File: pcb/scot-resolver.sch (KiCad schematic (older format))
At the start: 8 parts, among them J1 Conn_01x02_Female, J2 Conn_01x02_Female, J3 Conn_01x02_Female, J4 Conn_01x03_Female, J5 Conn_01x03_Female, J6 Conn_01x03_Female

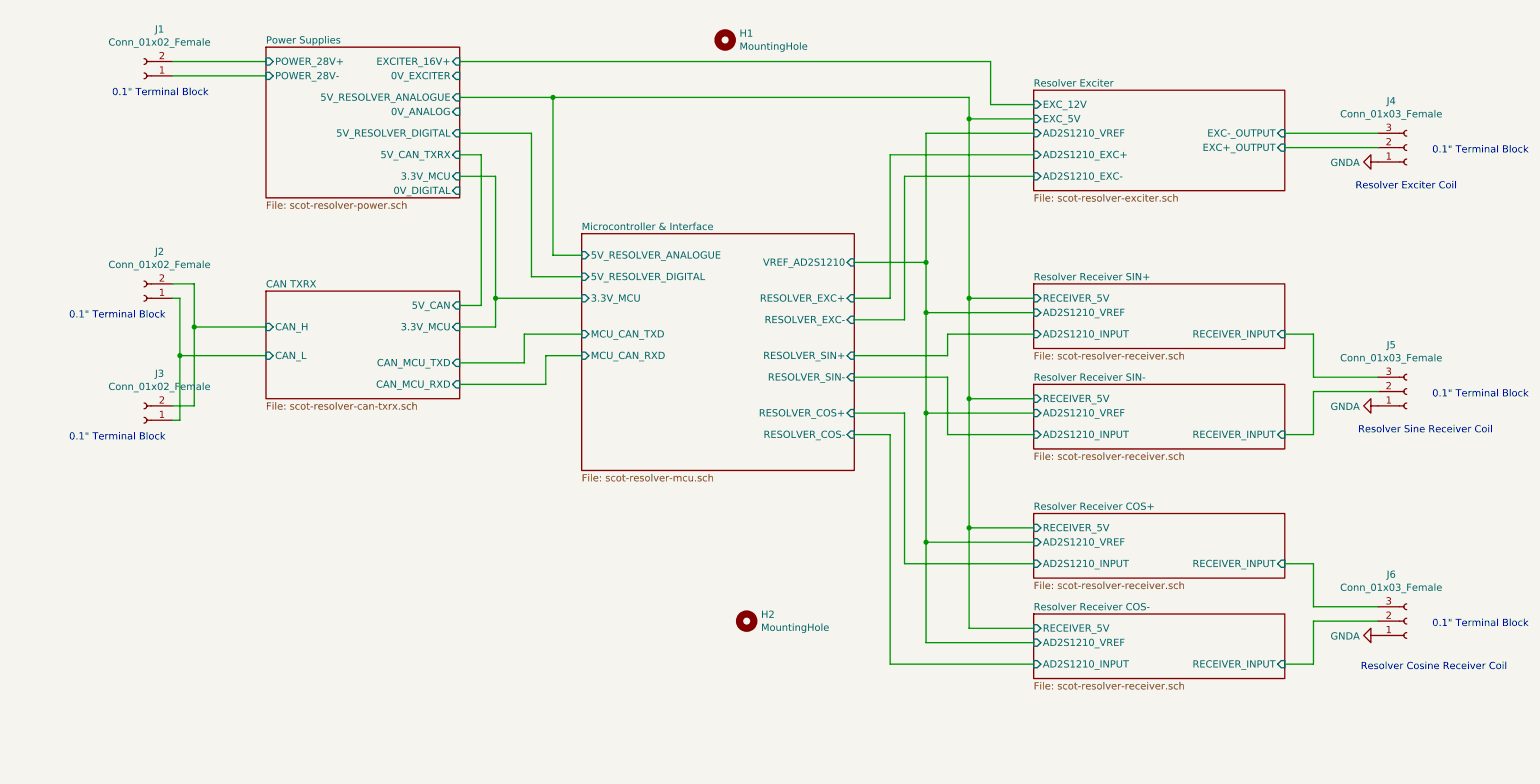
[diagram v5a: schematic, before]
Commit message: pcb: V2 schematic updates (PCB still to do).
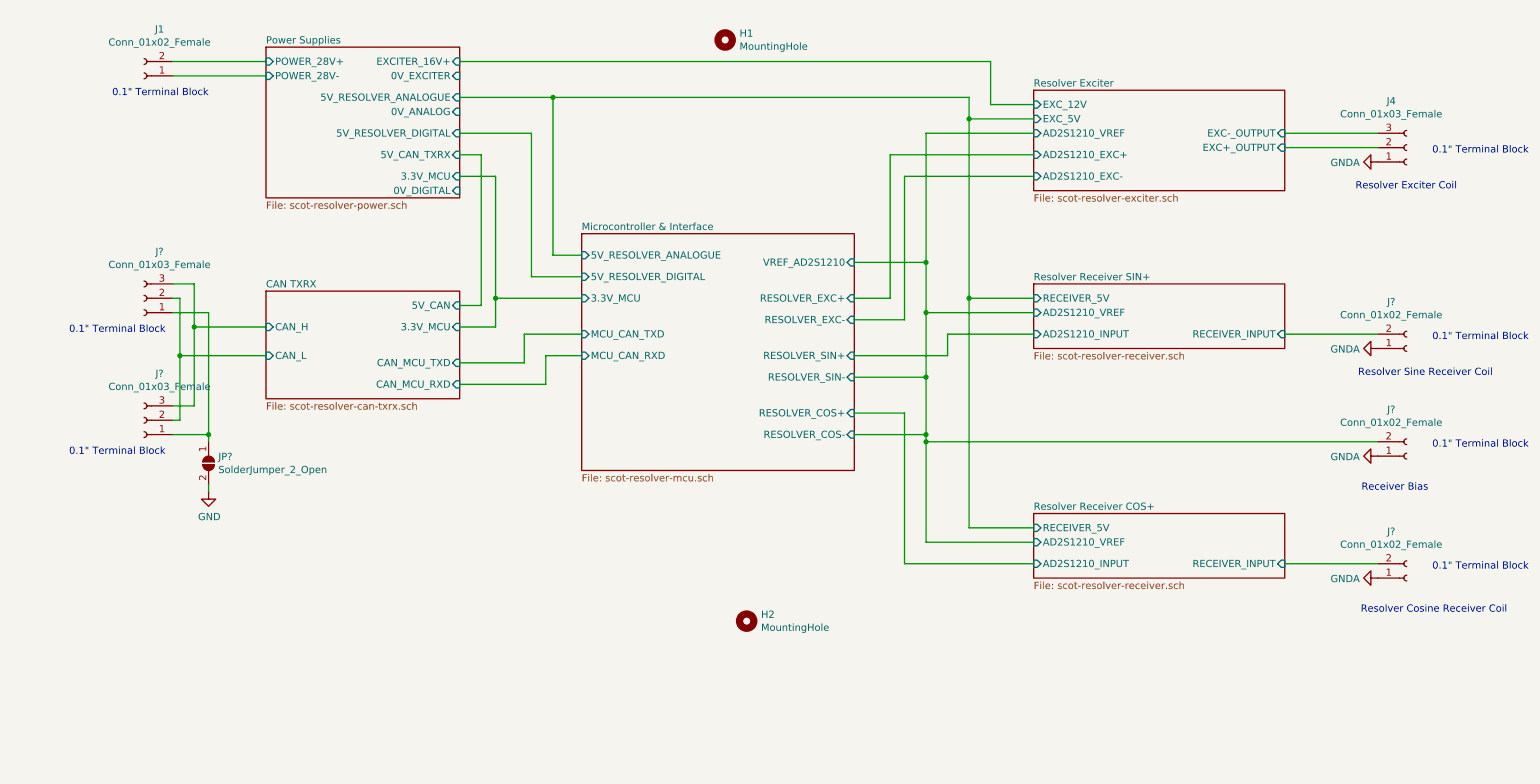
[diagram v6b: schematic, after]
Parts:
- removed J2, J3: Conn_01x02_Female, TerminalBlock_TE-Connectivity:TerminalBlock_TE_282834-2_1x02_P2.54mm_Horizontal, symbol Connector:Conn_01x02_Female
- removed J5, J6: Conn_01x03_Female, TerminalBlock_TE-Connectivity:TerminalBlock_TE_282834-3_1x03_P2.54mm_Horizontal, symbol Connector:Conn_01x03_Female
- added J? (x3): Conn_01x02_Female, TerminalBlock_TE-Connectivity:TerminalBlock_TE_282834-2_1x02_P2.54mm_Horizontal, symbol Connector:Conn_01x02_Female
- added J? (x2): Conn_01x03_Female, TerminalBlock_TE-Connectivity:TerminalBlock_TE_282834-3_1x03_P2.54mm_Horizontal, symbol Connector:Conn_01x03_Female
- added JP?: SolderJumper_2_Open, symbol Jumper:SolderJumper_2_Open
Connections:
- net CAN TXRX/CAN_H: now also J?.3 (Pin_3), J?.3 (Pin_3)
- net CAN TXRX/CAN_L: now also J?.2 (Pin_2), J?.2 (Pin_2)
- net GNDA: now also J?.1 (Pin_1), J?.1 (Pin_1), J?.1 (Pin_1)
- net Microcontroller & Interface/RESOLVER_COS-: now also J?.2 (Pin_2)
- net Resolver Receiver COS+/RECEIVER_INPUT: now also J?.2 (Pin_2)
- net Resolver Receiver SIN+/RECEIVER_INPUT: now also J?.2 (Pin_2)
- new net: J?.1 (Pin_1), J?.1 (Pin_1), JP?.1 (A)
- new net GND: JP?.2 (B)
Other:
- note added: "Receiver Bias"
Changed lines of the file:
@@
 $Descr A4 11693 8268
 encoding utf-8
-Sheet 1 9
+Sheet 1 7
 Title ""
 Date ""
@@
 Comment4 ""
 $EndDescr
-$Comp
-L Connector:Conn_01x02_Female J2
-U 1 1 5E03E563
-P 1350 2700
-F 0 "J2" H 1242 2375 50  0000 C CNN
-F 1 "Conn_01x02_Female" H 1242 2466 50  0000 C CNN
-F 2 "TerminalBlock_TE-Connectivity:TerminalBlock_TE_282834-2_1x02_P2.54mm_Horizontal" H 1350 2700 50  0001 C CNN
-F 3 "~" H 1350 2700 50  0001 C CNN
-	1    1350 2700
-	-1   0    0    1
-$EndComp
-$Comp
-L Connector:Conn_01x02_Female J3
-U 1 1 5E03F192
-P 1350 3550
-F 0 "J3" H 1242 3225 50  0000 C CNN
-F 1 "Conn_01x02_Female" H 1242 3316 50  0000 C CNN
-F 2 "TerminalBlock_TE-Connectivity:TerminalBlock_TE_282834-2_1x02_P2.54mm_Horizontal" H 1350 3550 50  0001 C CNN
-F 3 "~" H 1350 3550 50  0001 C CNN
-	1    1350 3550
-	-1   0    0    1
-$EndComp
 Wire Wire Line
 	1550 3450 1700 3450
@@
 	9300 1650 9950 1650
 $Sheet
-S 7550 3300 1750 450
-U 5E46BA7D
-F0 "Resolver Receiver SIN-" 50
-F1 "scot-resolver-receiver.sch" 50
-F2 "RECEIVER_INPUT" I R 9300 3650 50
-F3 "AD2S1210_VREF" I L 7550 3500 50
-F4 "AD2S1210_INPUT" I L 7550 3650 50
-F5 "RECEIVER_5V" I L 7550 3400 50
-$EndSheet
-$Sheet
 S 7550 4200 1750 450
 U 5E46F57D
@@
 F5 "RECEIVER_5V" I L 7550 4300 50
 $EndSheet
-$Sheet
-S 7550 4900 1750 450
-U 5E46F583
-F0 "Resolver Receiver COS-" 50
-F1 "scot-resolver-receiver.sch" 50
-F2 "RECEIVER_INPUT" I R 9300 5250 50
-F3 "AD2S1210_VREF" I L 7550 5100 50
-F4 "AD2S1210_INPUT" I L 7550 5250 50
-F5 "RECEIVER_5V" I L 7550 5000 50
-$EndSheet
-Wire Wire Line
-	9500 3250 9500 2950
-Wire Wire Line
-	9500 2950 9300 2950
-Wire Wire Line
-	9500 3350 9500 3650
-Wire Wire Line
-	9500 3650 9300 3650
-Wire Wire Line
-	9500 4850 9500 4550
-Wire Wire Line
-	9500 4550 9300 4550
-Wire Wire Line
-	9500 4950 9500 5250
-Wire Wire Line
-	9500 5250 9300 5250
 $Sheet
 S 2200 2650 1350 750
@@
 	7100 2700 7550 2700
 Connection ~ 7100 1450
-Wire Wire Line
-	7100 2700 7100 3400
-Wire Wire Line
-	7100 3400 7550 3400
 Connection ~ 7100 2700
 Wire Wire Line
-	7100 3400 7100 4300
-Wire Wire Line
 	7100 4300 7550 4300
-Connection ~ 7100 3400
-Wire Wire Line
-	7100 4300 7100 5000
-Wire Wire Line
-	7100 5000 7550 5000
-Connection ~ 7100 4300
 $Sheet
 S 4400 2250 1900 1650
@@
 	6800 2800 7550 2800
 Connection ~ 6800 2450
-Wire Wire Line
-	6800 2800 6800 3500
-Wire Wire Line
-	6800 3500 7550 3500
 Connection ~ 6800 2800
 Wire Wire Line
-	6800 3500 6800 4400
-Wire Wire Line
 	6800 4400 7550 4400
-Connection ~ 6800 3500
-Wire Wire Line
-	6800 4400 6800 5100
-Wire Wire Line
-	6800 5100 7550 5100
-Connection ~ 6800 4400
 Wire Wire Line
 	6300 3500 6650 3500
@@
 Wire Wire Line
 	6650 4550 7550 4550
-Wire Wire Line
-	7550 5250 6550 5250
-Wire Wire Line
-	6550 5250 6550 3650
-Wire Wire Line
-	6550 3650 6300 3650
-Wire Wire Line
-	6300 3250 6950 3250
-Wire Wire Line
-	6950 3250 6950 3650
-Wire Wire Line
-	6950 3650 7550 3650
 Wire Wire Line
 	6300 3100 6950 3100
@@
 Text Notes 10500 1950 2    50   ~ 0
 Resolver Exciter Coil
-Text Notes 10750 3650 2    50   ~ 0
+Text Notes 10750 3250 2    50   ~ 0
 Resolver Sine Receiver Coil
-Text Notes 10850 5300 2    50   ~ 0
+Text Notes 10850 4900 2    50   ~ 0
 Resolver Cosine Receiver Coil
 Wire Wire Line
@@
 	0    1    1    0
 $EndComp
-Wire Wire Line
-	9500 3250 9950 3250
-Wire Wire Line
-	9950 3350 9500 3350
 $Comp
 L power:GNDA #PWR0102
 U 1 1 5E62D3A8
-P 9950 3450
-F 0 "#PWR0102" H 9950 3200 50  0001 C CNN
-F 1 "GNDA" V 9955 3323 50  0000 R CNN
-F 2 "" H 9950 3450 50  0001 C CNN
-F 3 "" H 9950 3450 50  0001 C CNN
-	1    9950 3450
+P 9950 3050
+F 0 "#PWR0102" H 9950 2800 50  0001 C CNN
+F 1 "GNDA" V 9955 2923 50  0000 R CNN
+F 2 "" H 9950 3050 50  0001 C CNN
+F 3 "" H 9950 3050 50  0001 C CNN
+	1    9950 3050
 	0    1    1    0
 $EndComp
@@
 L power:GNDA #PWR0103
 U 1 1 5E638B63
-P 9950 5050
-F 0 "#PWR0103" H 9950 4800 50  0001 C CNN
-F 1 "GNDA" V 9955 4923 50  0000 R CNN
-F 2 "" H 9950 5050 50  0001 C CNN
-F 3 "" H 9950 5050 50  0001 C CNN
-	1    9950 5050
+P 9950 4650
+F 0 "#PWR0103" H 9950 4400 50  0001 C CNN
+F 1 "GNDA" V 9955 4523 50  0000 R CNN
+F 2 "" H 9950 4650 50  0001 C CNN
+F 3 "" H 9950 4650 50  0001 C CNN
+	1    9950 4650
 	0    1    1    0
 $EndComp
-Wire Wire Line
-	9950 4950 9500 4950
-Wire Wire Line
-	9500 4850 9950 4850
 $Comp
 L Connector:Conn_01x03_Female J4
@@
 $EndComp
 $Comp
-L Connector:Conn_01x03_Female J5
-U 1 1 5E642718
-P 10150 3350
-F 0 "J5" H 10042 3025 50  0000 C CNN
-F 1 "Conn_01x03_Female" H 10042 3116 50  0000 C CNN
-F 2 "TerminalBlock_TE-Connectivity:TerminalBlock_TE_282834-3_1x03_P2.54mm_Horizontal" H 10150 3350 50  0001 C CNN
-F 3 "~" H 10150 3350 50  0001 C CNN
-	1    10150 3350
-	1    0    0    1
-$EndComp
-$Comp
-L Connector:Conn_01x03_Female J6
-U 1 1 5E642DF1
-P 10150 4950
-F 0 "J6" H 10042 4625 50  0000 C CNN
-F 1 "Conn_01x03_Female" H 10042 4716 50  0000 C CNN
-F 2 "TerminalBlock_TE-Connectivity:TerminalBlock_TE_282834-3_1x03_P2.54mm_Horizontal" H 10150 4950 50  0001 C CNN
-F 3 "~" H 10150 4950 50  0001 C CNN
-	1    10150 4950
-	1    0    0    1
-$EndComp
-$Comp
 L Mechanical:MountingHole H1
 U 1 1 5E4FCB16
@@
 	1    0    0    -1
 $EndComp
-Text Notes 1500 2850 2    50   ~ 0
-0.1" Terminal Block
-Text Notes 1500 3700 2    50   ~ 0
+Text Notes 1500 2950 2    50   ~ 0
+0.1" Terminal Block
+Text Notes 1500 3800 2    50   ~ 0
 0.1" Terminal Block
 Text Notes 11000 1700 2    50   ~ 0
 0.1" Terminal Block
-Text Notes 11000 3400 2    50   ~ 0
-0.1" Terminal Block
-Text Notes 11000 5000 2    50   ~ 0
-0.1" Terminal Block
+Text Notes 11000 3000 2    50   ~ 0
+0.1" Terminal Block
+Text Notes 11000 4600 2    50   ~ 0
+0.1" Terminal Block
+$Comp
+L Connector:Conn_01x02_Female J?
+U 1 1 5EAD507C
+P 10150 3050
+F 0 "J?" H 10042 2725 50  0000 C CNN
+F 1 "Conn_01x02_Female" H 10042 2816 50  0000 C CNN
+F 2 "TerminalBlock_TE-Connectivity:TerminalBlock_TE_282834-2_1x02_P2.54mm_Horizontal" H 10150 3050 50  0001 C CNN
+F 3 "~" H 10150 3050 50  0001 C CNN
+	1    10150 3050
+	1    0    0    1
+$EndComp
+Wire Wire Line
+	9300 2950 9950 2950
+$Comp
+L Connector:Conn_01x02_Female J?
+U 1 1 5EADF09C
+P 10150 4650
+F 0 "J?" H 10042 4325 50  0000 C CNN
+F 1 "Conn_01x02_Female" H 10042 4416 50  0000 C CNN
+F 2 "TerminalBlock_TE-Connectivity:TerminalBlock_TE_282834-2_1x02_P2.54mm_Horizontal" H 10150 4650 50  0001 C CNN
+F 3 "~" H 10150 4650 50  0001 C CNN
+	1    10150 4650
+	1    0    0    1
+$EndComp
+Wire Wire Line
+	9300 4550 9950 4550
+Text Notes 10300 4050 2    50   ~ 0
+Receiver Bias
+$Comp
+L power:GNDA #PWR?
+U 1 1 5EAE45AD
+P 9950 3800
+F 0 "#PWR?" H 9950 3550 50  0001 C CNN
+F 1 "GNDA" V 9955 3673 50  0000 R CNN
+F 2 "" H 9950 3800 50  0001 C CNN
+F 3 "" H 9950 3800 50  0001 C CNN
+	1    9950 3800
+	0    1    1    0
+$EndComp
+Text Notes 11000 3750 2    50   ~ 0
+0.1" Terminal Block
+$Comp
+L Connector:Conn_01x02_Female J?
+U 1 1 5EAE45B8
+P 10150 3800
+F 0 "J?" H 10042 3475 50  0000 C CNN
+F 1 "Conn_01x02_Female" H 10042 3566 50  0000 C CNN
+F 2 "TerminalBlock_TE-Connectivity:TerminalBlock_TE_282834-2_1x02_P2.54mm_Horizontal" H 10150 3800 50  0001 C CNN
+F 3 "~" H 10150 3800 50  0001 C CNN
+	1    10150 3800
+	1    0    0    1
+$EndComp
+Wire Wire Line
+	7100 2700 7100 4300
+Wire Wire Line
+	6800 2800 6800 3250
+Wire Wire Line
+	6800 3700 9950 3700
+Connection ~ 6800 3700
+Wire Wire Line
+	6800 3700 6800 4400
+Wire Wire Line
+	6300 3650 6800 3650
+Connection ~ 6800 3650
+Wire Wire Line
+	6800 3650 6800 3700
+Wire Wire Line
+	6300 3250 6800 3250
+Connection ~ 6800 3250
+Wire Wire Line
+	6800 3250 6800 3650
+$Comp
+L Connector:Conn_01x03_Female J?
+U 1 1 5EAEEF38
+P 1350 2700
+F 0 "J?" H 1242 2375 50  0000 C CNN
+F 1 "Conn_01x03_Female" H 1242 2466 50  0000 C CNN
+F 2 "TerminalBlock_TE-Connectivity:TerminalBlock_TE_282834-3_1x03_P2.54mm_Horizontal" H 1350 2700 50  0001 C CNN
+F 3 "~" H 1350 2700 50  0001 C CNN
+	1    1350 2700
+	-1   0    0    1
+$EndComp
+$Comp
+L Connector:Conn_01x03_Female J?
+U 1 1 5EAF204B
+P 1350 3550
+F 0 "J?" H 1242 3225 50  0000 C CNN
+F 1 "Conn_01x03_Female" H 1242 3316 50  0000 C CNN
+F 2 "TerminalBlock_TE-Connectivity:TerminalBlock_TE_282834-3_1x03_P2.54mm_Horizontal" H 1350 3550 50  0001 C CNN
+F 3 "~" H 1350 3550 50  0001 C CNN
+	1    1350 3550
+	-1   0    0    1
+$EndComp
+Wire Wire Line
+	1550 2800 1800 2800
+Wire Wire Line
+	1800 2800 1800 3650
+Wire Wire Line
+	1800 3650 1550 3650
+$Comp
+L Jumper:SolderJumper_2_Open JP?
+U 1 1 5EAF4284
+P 1800 3850
+F 0 "JP?" V 1754 3918 50  0000 L CNN
+F 1 "SolderJumper_2_Open" V 1845 3918 50  0000 L CNN
+F 2 "" H 1800 3850 50  0001 C CNN
+F 3 "~" H 1800 3850 50  0001 C CNN
+	1    1800 3850
+	0    1    1    0
+$EndComp
+$Comp
+L power:GND #PWR?
+U 1 1 5EAF4C43
+P 1800 4050
+F 0 "#PWR?" H 1800 3800 50  0001 C CNN
+F 1 "GND" H 1805 3877 50  0000 C CNN
+F 2 "" H 1800 4050 50  0001 C CNN
+F 3 "" H 1800 4050 50  0001 C CNN
+	1    1800 4050
+	1    0    0    -1
+$EndComp
+Wire Wire Line
+	1800 4050 1800 4000
+Wire Wire Line
+	1800 3700 1800 3650
+Connection ~ 1800 3650
 $EndSCHEMATC

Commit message: pcb: Add 10u to VREF, all 0402->0603
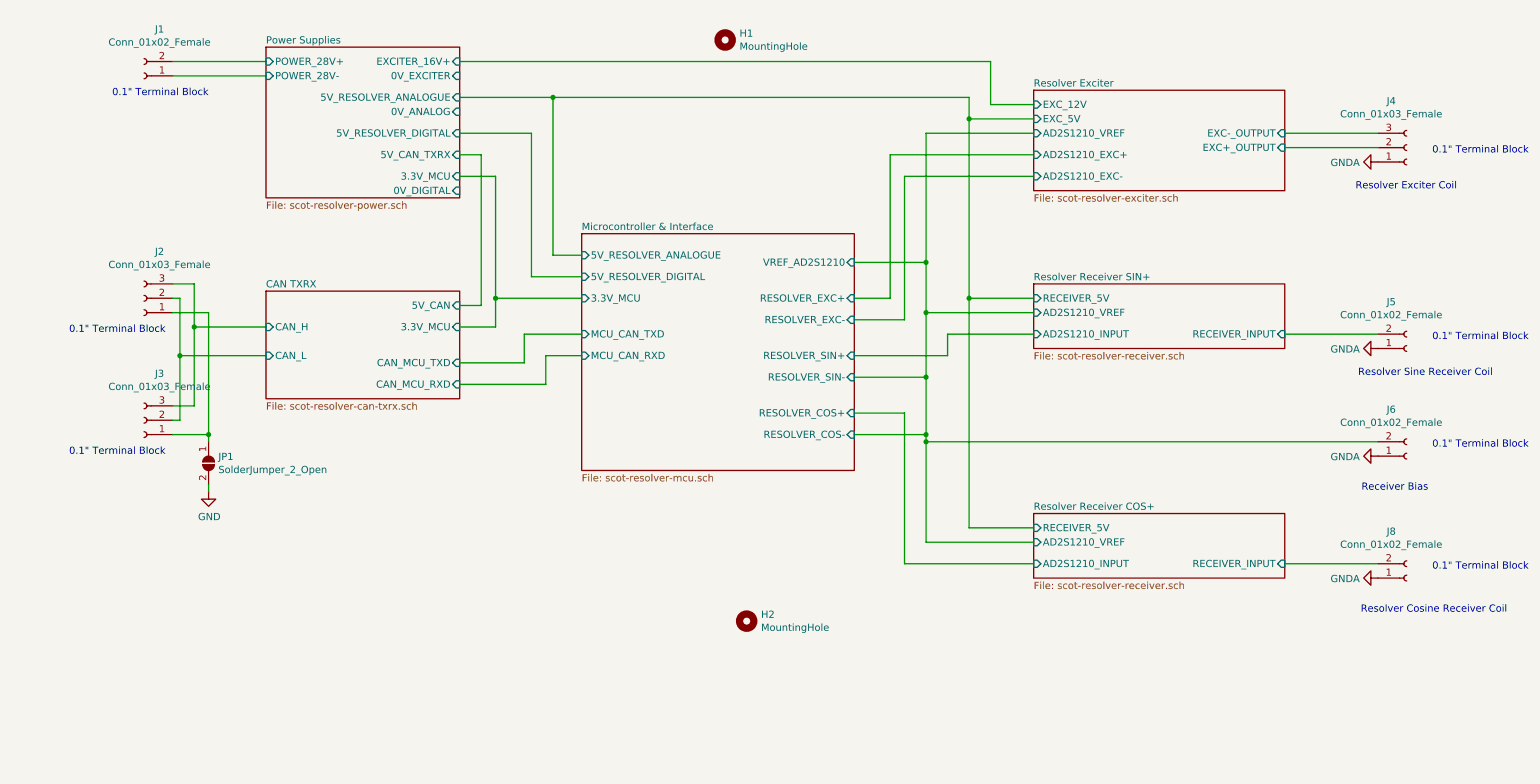
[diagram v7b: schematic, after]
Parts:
- JP1: renamed from JP?; footprint (none) -> Jumper:SolderJumper-2_P1.3mm_Open_RoundedPad1.0x1.5mm
- gave numbers to parts that had none: 5
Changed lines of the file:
@@
 0.1" Terminal Block
 $Comp
-L Connector:Conn_01x02_Female J?
+L Connector:Conn_01x02_Female J5
 U 1 1 5EAD507C
 P 10150 3050
-F 0 "J?" H 10042 2725 50  0000 C CNN
+F 0 "J5" H 10042 2725 50  0000 C CNN
 F 1 "Conn_01x02_Female" H 10042 2816 50  0000 C CNN
 F 2 "TerminalBlock_TE-Connectivity:TerminalBlock_TE_282834-2_1x02_P2.54mm_Horizontal" H 10150 3050 50  0001 C CNN
@@
 	9300 2950 9950 2950
 $Comp
-L Connector:Conn_01x02_Female J?
+L Connector:Conn_01x02_Female J8
 U 1 1 5EADF09C
 P 10150 4650
-F 0 "J?" H 10042 4325 50  0000 C CNN
+F 0 "J8" H 10042 4325 50  0000 C CNN
 F 1 "Conn_01x02_Female" H 10042 4416 50  0000 C CNN
 F 2 "TerminalBlock_TE-Connectivity:TerminalBlock_TE_282834-2_1x02_P2.54mm_Horizontal" H 10150 4650 50  0001 C CNN
@@
 Receiver Bias
 $Comp
-L power:GNDA #PWR?
+L power:GNDA #PWR0113
 U 1 1 5EAE45AD
 P 9950 3800
-F 0 "#PWR?" H 9950 3550 50  0001 C CNN
+F 0 "#PWR0113" H 9950 3550 50  0001 C CNN
 F 1 "GNDA" V 9955 3673 50  0000 R CNN
 F 2 "" H 9950 3800 50  0001 C CNN
@@
 0.1" Terminal Block
 $Comp
-L Connector:Conn_01x02_Female J?
+L Connector:Conn_01x02_Female J6
 U 1 1 5EAE45B8
 P 10150 3800
-F 0 "J?" H 10042 3475 50  0000 C CNN
+F 0 "J6" H 10042 3475 50  0000 C CNN
 F 1 "Conn_01x02_Female" H 10042 3566 50  0000 C CNN
 F 2 "TerminalBlock_TE-Connectivity:TerminalBlock_TE_282834-2_1x02_P2.54mm_Horizontal" H 10150 3800 50  0001 C CNN
@@
 	6800 3250 6800 3650
 $Comp
-L Connector:Conn_01x03_Female J?
+L Connector:Conn_01x03_Female J2
 U 1 1 5EAEEF38
 P 1350 2700
-F 0 "J?" H 1242 2375 50  0000 C CNN
+F 0 "J2" H 1242 2375 50  0000 C CNN
 F 1 "Conn_01x03_Female" H 1242 2466 50  0000 C CNN
 F 2 "TerminalBlock_TE-Connectivity:TerminalBlock_TE_282834-3_1x03_P2.54mm_Horizontal" H 1350 2700 50  0001 C CNN
@@
 $EndComp
 $Comp
-L Connector:Conn_01x03_Female J?
+L Connector:Conn_01x03_Female J3
 U 1 1 5EAF204B
 P 1350 3550
-F 0 "J?" H 1242 3225 50  0000 C CNN
+F 0 "J3" H 1242 3225 50  0000 C CNN
 F 1 "Conn_01x03_Female" H 1242 3316 50  0000 C CNN
 F 2 "TerminalBlock_TE-Connectivity:TerminalBlock_TE_282834-3_1x03_P2.54mm_Horizontal" H 1350 3550 50  0001 C CNN
@@
 	1800 3650 1550 3650
 $Comp
-L Jumper:SolderJumper_2_Open JP?
+L Jumper:SolderJumper_2_Open JP1
 U 1 1 5EAF4284
 P 1800 3850
-F 0 "JP?" V 1754 3918 50  0000 L CNN
+F 0 "JP1" V 1754 3918 50  0000 L CNN
 F 1 "SolderJumper_2_Open" V 1845 3918 50  0000 L CNN
-F 2 "" H 1800 3850 50  0001 C CNN
+F 2 "Jumper:SolderJumper-2_P1.3mm_Open_RoundedPad1.0x1.5mm" H 1800 3850 50  0001 C CNN
 F 3 "~" H 1800 3850 50  0001 C CNN
 	1    1800 3850
@@
 $EndComp
 $Comp
-L power:GND #PWR?
+L power:GND #PWR0114
 U 1 1 5EAF4C43
 P 1800 4050
-F 0 "#PWR?" H 1800 3800 50  0001 C CNN
+F 0 "#PWR0114" H 1800 3800 50  0001 C CNN
 F 1 "GND" H 1805 3877 50  0000 C CNN
 F 2 "" H 1800 4050 50  0001 C CNN
